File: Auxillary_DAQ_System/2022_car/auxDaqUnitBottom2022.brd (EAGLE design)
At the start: 121.9 x 193 mm, 120 parts, among them IC1 ADS8332IBPWR, IC2 ADS8332IBPWR, IC3 ADS8332IBPWR, IC4 XBEE, IC6 REG_3V3_LM3940, U1 REF5040AIDR, U3 TS1874IPT, U4 TS1874IPT, U5 TS1874IPT, U6 TS1874IPT, U7 TS1874IPT, U8 TS1874IPT

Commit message: Added missing capacitor values
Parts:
- C33, C34, C35, C36, C37, C38: value (none) -> .1uf
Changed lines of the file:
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@@
 <drawing>
 <settings>
-<setting alwaysvectorfont="yes"/>
+<setting alwaysvectorfont="no"/>
 <setting verticaltext="up"/>
 </settings>
@@
 <attribute name="VALUE" x="24.765" y="81.8515" size="1.27" layer="27" rot="R90"/>
 </element>
-<element name="C33" library="GTOR - Passive Components" package="C0603" package3d_urn="urn:adsk.eagle:package:23616/2" value="" x="21.59" y="163.195" smashed="yes" rot="R90">
+<element name="C33" library="GTOR - Passive Components" package="C0603" package3d_urn="urn:adsk.eagle:package:23616/2" value=".1uf" x="21.59" y="163.195" smashed="yes" rot="R90">
 <attribute name="NAME" x="20.955" y="162.56" size="1.27" layer="25" rot="R90"/>
 <attribute name="POPULARITY" value="73" x="21.59" y="163.195" size="1.778" layer="27" rot="R90" display="off"/>
@@
 <attribute name="VALUE" x="23.495" y="162.56" size="1.27" layer="27" rot="R90"/>
 </element>
-<element name="C34" library="GTOR - Passive Components" package="C0603" package3d_urn="urn:adsk.eagle:package:23616/2" value="" x="21.59" y="79.375" smashed="yes" rot="R90">
+<element name="C34" library="GTOR - Passive Components" package="C0603" package3d_urn="urn:adsk.eagle:package:23616/2" value=".1uf" x="21.59" y="79.375" smashed="yes" rot="R90">
 <attribute name="NAME" x="20.955" y="78.74" size="1.27" layer="25" rot="R90"/>
 <attribute name="POPULARITY" value="73" x="21.59" y="79.375" size="1.778" layer="27" rot="R90" display="off"/>
@@
 <attribute name="VALUE" x="23.495" y="78.74" size="1.27" layer="27" rot="R90"/>
 </element>
-<element name="C35" library="GTOR - Passive Components" package="C0603" package3d_urn="urn:adsk.eagle:package:23616/2" value="" x="21.59" y="118.745" smashed="yes" rot="R90">
+<element name="C35" library="GTOR - Passive Components" package="C0603" package3d_urn="urn:adsk.eagle:package:23616/2" value=".1uf" x="21.59" y="118.745" smashed="yes" rot="R90">
 <attribute name="NAME" x="20.955" y="118.11" size="1.27" layer="25" rot="R90"/>
 <attribute name="POPULARITY" value="73" x="21.59" y="118.745" size="1.778" layer="27" rot="R90" display="off"/>
@@
 <attribute name="VALUE" x="23.495" y="118.11" size="1.27" layer="27" rot="R90"/>
 </element>
-<element name="C36" library="GTOR - Passive Components" package="C0603" package3d_urn="urn:adsk.eagle:package:23616/2" value="" x="23.8125" y="163.195" smashed="yes" rot="R90">
+<element name="C36" library="GTOR - Passive Components" package="C0603" package3d_urn="urn:adsk.eagle:package:23616/2" value=".1uf" x="23.8125" y="163.195" smashed="yes" rot="R90">
 <attribute name="NAME" x="23.1775" y="162.56" size="1.27" layer="25" rot="R90"/>
 <attribute name="POPULARITY" value="73" x="23.8125" y="163.195" size="1.778" layer="27" rot="R90" display="off"/>
@@
 <attribute name="VALUE" x="25.7175" y="162.56" size="1.27" layer="27" rot="R90"/>
 </element>
-<element name="C37" library="GTOR - Passive Components" package="C0603" package3d_urn="urn:adsk.eagle:package:23616/2" value="" x="23.8125" y="79.375" smashed="yes" rot="R90">
+<element name="C37" library="GTOR - Passive Components" package="C0603" package3d_urn="urn:adsk.eagle:package:23616/2" value=".1uf" x="23.8125" y="79.375" smashed="yes" rot="R90">
 <attribute name="NAME" x="23.1775" y="78.74" size="1.27" layer="25" rot="R90"/>
 <attribute name="POPULARITY" value="73" x="23.8125" y="79.375" size="1.778" layer="27" rot="R90" display="off"/>
@@
 <attribute name="VALUE" x="25.7175" y="78.74" size="1.27" layer="27" rot="R90"/>
 </element>
-<element name="C38" library="GTOR - Passive Components" package="C0603" package3d_urn="urn:adsk.eagle:package:23616/2" value="" x="23.8125" y="118.745" smashed="yes" rot="R90">
+<element name="C38" library="GTOR - Passive Components" package="C0603" package3d_urn="urn:adsk.eagle:package:23616/2" value=".1uf" x="23.8125" y="118.745" smashed="yes" rot="R90">
 <attribute name="NAME" x="23.1775" y="118.11" size="1.27" layer="25" rot="R90"/>
 <attribute name="POPULARITY" value="73" x="23.8125" y="118.745" size="1.778" layer="27" rot="R90" display="off"/>

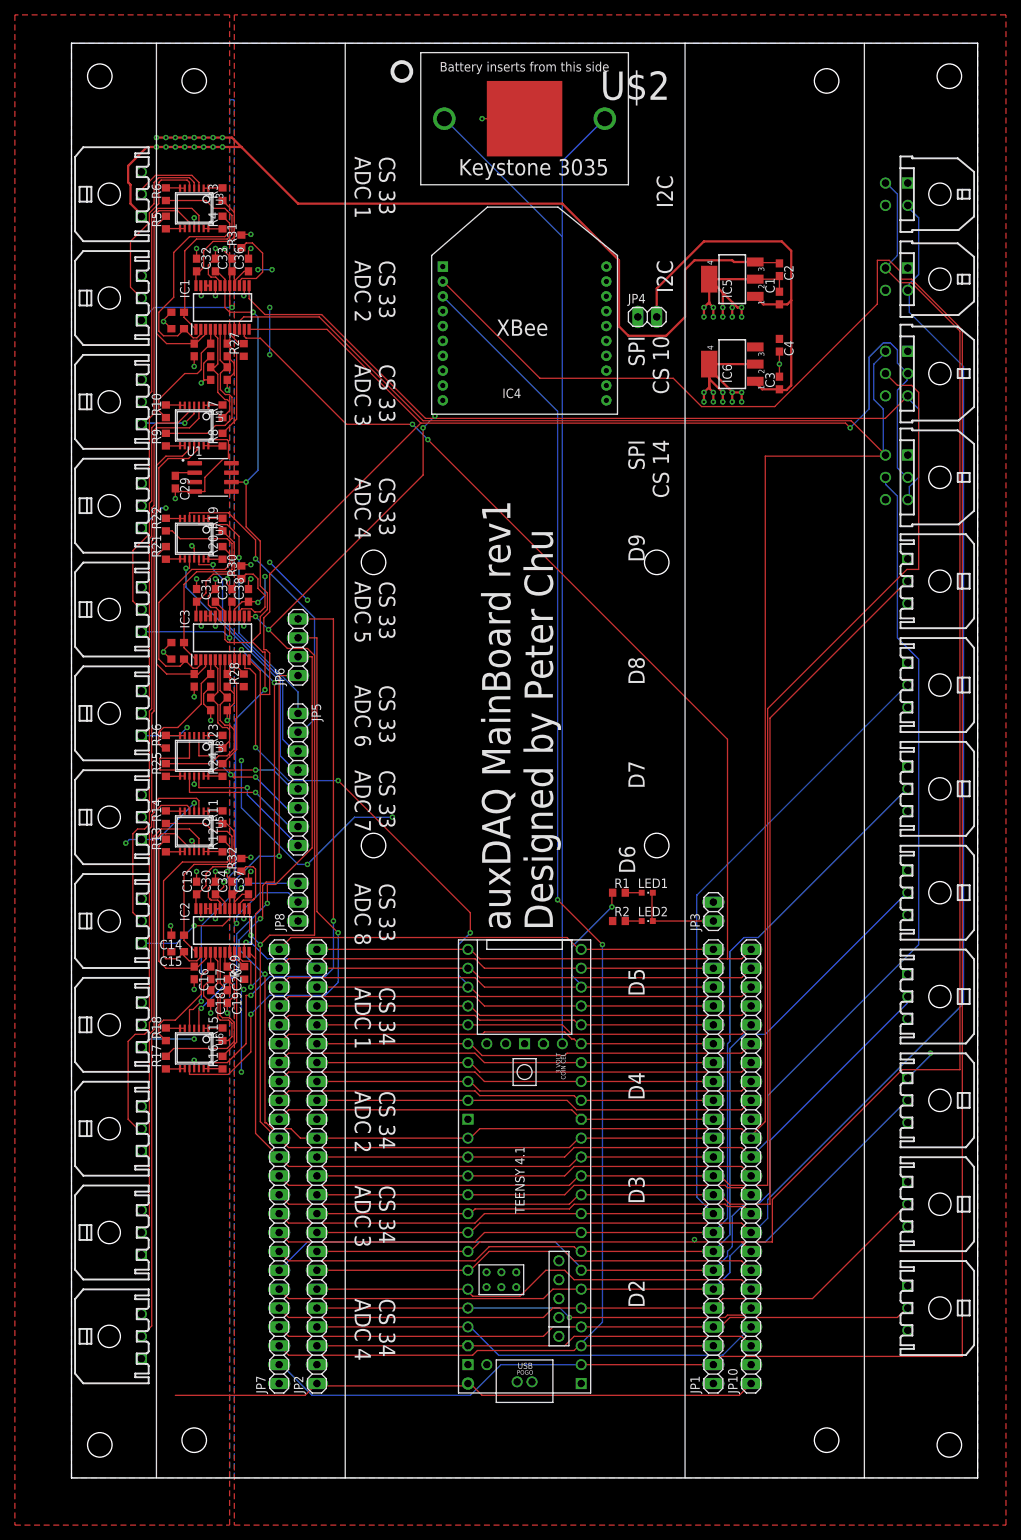
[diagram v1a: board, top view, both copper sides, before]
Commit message: Started changes for new Aux Daq
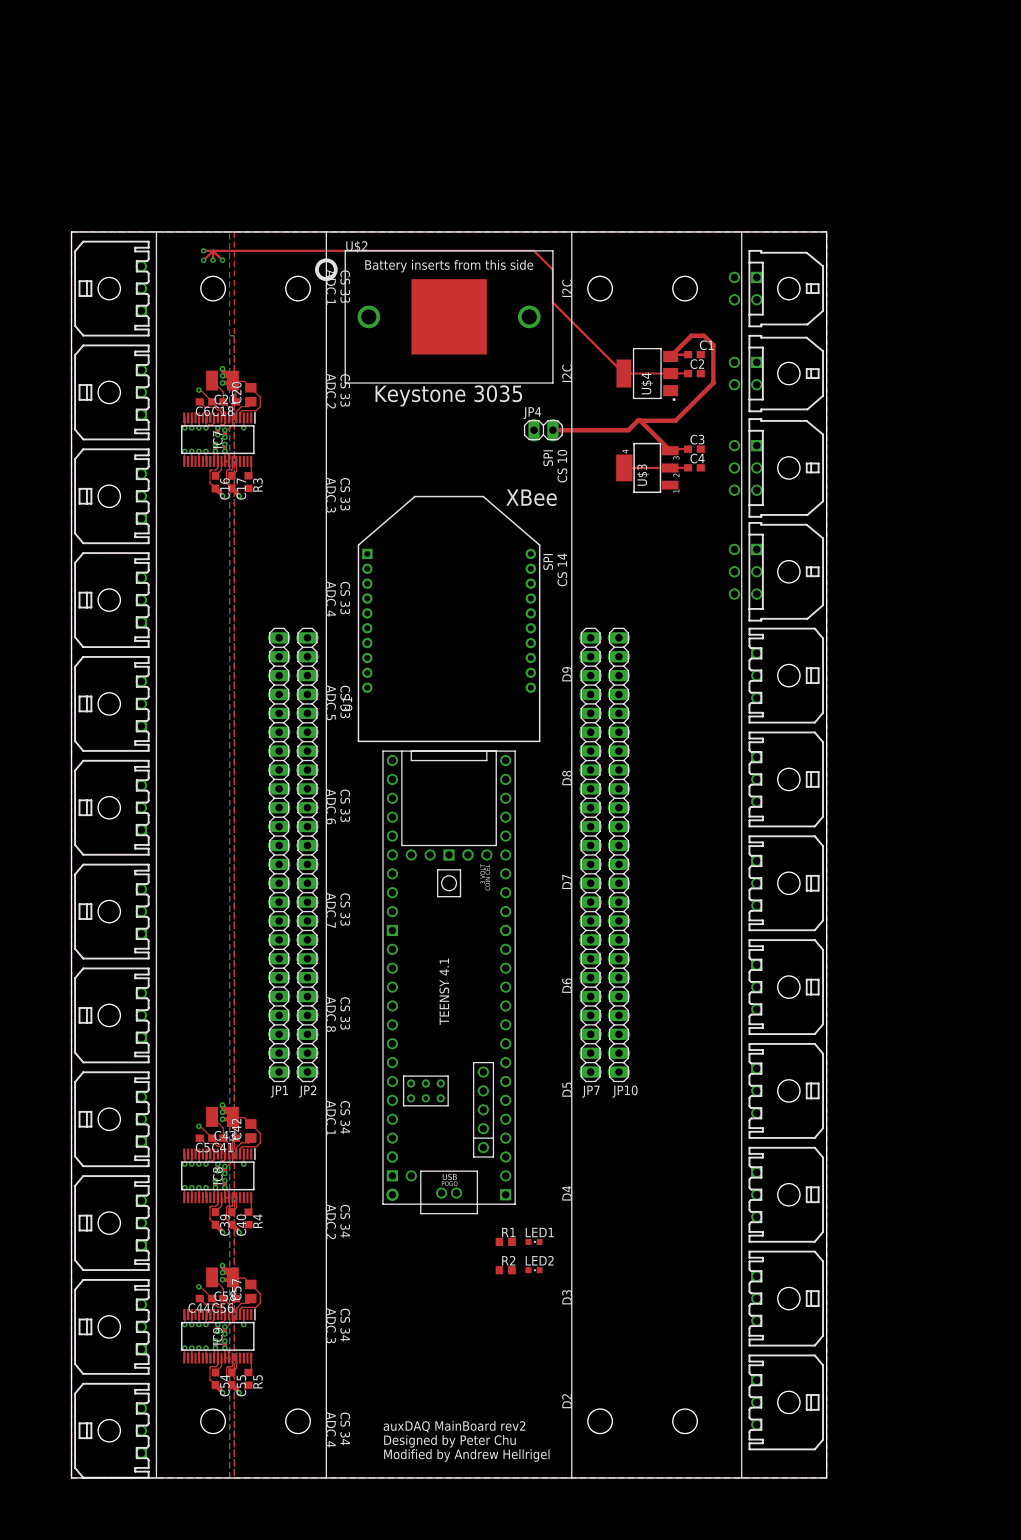
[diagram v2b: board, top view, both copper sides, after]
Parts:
- removed C10, C11, C12, C13, C14, C15, C19, C22, C23, C24, C25, C26, C27, C28, C7, C8, C9: 1nf, GTOR - Passive Components:C0603
- removed C29: 1uf, GTOR - Passive Components:C0603
- removed C30, C31, C32: 10uf, GTOR - Passive Components:C0603
- removed C33, C34, C35, C36, C37, C38: .1uf, GTOR - Passive Components:C0603
- removed IC1, IC2, IC3: ADS8332IBPWR, GTOR - Active Components:SOP65P640X120-24N
- removed IC4: XBEE, GTOR - Microcontroller:XBEE
- removed IC5: (no value), GTOR - Active Components:SOT223
- removed IC6: REG_3V3_LM3940, GTOR - Active Components:SOT223
- removed JP3: (no value), GTOR - Connectors:1X02
- removed JP5: (no value), GTOR - Connectors:1X08
- removed JP6: (no value), GTOR - Connectors:1X04
- removed JP8: (no value), GTOR - Connectors:1X03
- removed R10, R11, R12, R13, R14, R15, R16, R17, R18, R19, R20, R21, R22, R23, R24, R25, R26, R6, R7, R8, R9: 20, GTOR - Passive Components:R0603
- removed R27, R28, R29, R30, R31, R32: 10k, GTOR - Passive Components:R0603
- removed U3, U4, U5, U6, U7, U8: TS1874IPT, GTOR - Active Components:TSSOP14
- added C39, C41, C44, C54, C56: 1uF, GTOR - Passive Components:C0603
- added C40, C55: 10uF, GTOR - Passive Components:C0603
- added C42, C57: 10uF, GTOR - Passive Components:C0805
- added C43, C58: 22uF, GTOR - Passive Components:C1210
- added IC7, IC8, IC9: ADC_ADS8688IDBTR, GTOR - Active Components:SOP50P640X120-38N
- added U$3: REG_3V3_LMS8117A, GTOR - Active Components:SOT223
- added U$4: REG_5V_LDL1117S50R, GTOR - Active Components:SOT230P700X180-4N
- C16, C18, C5, C6: value 1nf -> 1uF
- C17: value 1nf -> 10uF
- C20: value 1nf -> 10uF; device GTOR - Passive Components:C0603 -> GTOR - Passive Components:C0805
- C21: value 1nf -> 22uF; device GTOR - Passive Components:C0603 -> GTOR - Passive Components:C1210
- R3, R4, R5: value 20 -> 10k
- U1: value REF5040AIDR -> XBEE_PRO_S3B; device GTOR - Active Components:SOIC127P599X175-8N -> GTOR - Microcontroller:XBEE_PRO_S3B
- moved R5 156.0 mm to (23.8, 13.3), turned to 270 degrees
- moved R4 134.0 mm to (23.8, 34.9), turned to 270 degrees
- moved C5 117.5 mm to (18.1, 45.7), turned to 180 degrees
- moved C18 80.1 mm to (21.3, 144.8), turned to 180 degrees
- moved C20 77.9 mm to (24.1, 145.7), turned to 90 degrees
- moved JP1 71.9 mm to (27.9, 83.8)
- moved C16 66.1 mm to (19.4, 134.0)
- moved C17 66.1 mm to (21.6, 134.0)
- moved JP7 59.3 mm to (69.8, 83.8)
- moved LED2 49.4 mm to (62.2, 27.9)
- moved R2 49.4 mm to (58.4, 27.9)
- moved LED1 49.4 mm to (62.2, 31.8)
- moved R1 49.4 mm to (58.4, 31.8)
- moved JP10 45.5 mm to (73.7, 83.8)
- moved JP2 41.9 mm to (31.8, 83.8)
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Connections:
- removed net IN1: C5.1, IC1.24, R3.1
- removed net IN10: C14.1, IC2.1, R14.1
- removed net IN11: C15.1, IC2.2, R12.2
- removed net IN12: C16.1, IC2.3, R13.2
- removed net IN13: C17.1, IC2.4, R18.1
- removed net IN14: C18.1, IC2.5, R15.1
- removed net IN15: C19.1, IC2.6, R17.2
- removed net IN16: C20.1, IC2.7, R16.2
- removed net IN17: C21.1, IC3.24, R19.1
- removed net IN18: C22.1, IC3.1, R22.1
- removed net IN19: C23.1, IC3.2, R20.2
- removed net IN2: C6.1, IC1.1, R6.1
- removed net IN20: C24.1, IC3.3, R21.2
- removed net IN21: C25.1, IC3.4, R26.1
- removed net IN22: C26.1, IC3.5, R23.1
- removed net IN23: C27.1, IC3.6, R25.2
- removed net IN24: C28.1, IC3.7, R24.2
- removed net IN3: C7.1, IC1.2, R4.2
- removed net IN4: C8.1, IC1.3, R5.2
- removed net IN5: C9.1, IC1.4, R10.1
- removed net IN6: C10.1, IC1.5, R7.1
- removed net IN7: C11.1, IC1.6, R9.2
- removed net IN8: C12.1, IC1.7, R8.2
- removed net IN9: C13.1, IC2.24, R11.1
- removed net N$10: IC1.8, R27.2
- removed net N$11: R7.2, U4.1, U4.2
- removed net N$12: R10.2, U4.6, U4.7
- removed net N$14: R8.1, U4.13, U4.14
- removed net N$15: IC3.8, R28.2
- removed net N$16: R11.2, U5.1, U5.2
- removed net N$18: R13.1, U5.8, U5.9
- removed net N$19: R12.1, U5.13, U5.14
- removed net N$20: IC2.8, R29.2
- removed net N$21: R15.2, U6.1, U6.2
- removed net N$22: R18.2, U6.6, U6.7
- removed net N$23: R17.1, U6.8, U6.9
- removed net N$24: R16.1, U6.13, U6.14
- removed net N$25: IC3.15, R30.1
- removed net N$26: R19.2, U7.1, U7.2
- removed net N$27: R22.2, U7.6, U7.7
- removed net N$29: R20.1, U7.13, U7.14
- removed net N$3: IC1.21, IC1.22
- removed net N$30: IC1.15, R31.1
- removed net N$33: R25.1, U8.8, U8.9
- removed net N$34: R24.1, U8.13, U8.14
- removed net N$35: IC2.15, R32.1
- removed net N$4: IC2.21, IC2.22
- removed net N$5: IC3.21, IC3.22
- removed net N$9: R4.1, U3.13, U3.14
- removed net REF+: C30.1, C31.1, C32.1, IC1.18, IC2.18, IC3.18, U1.6
- new net N$45: C57.1, IC9.5
- new net NC1: IC7.35
- new net NC2: IC8.35
- new net NC3: IC9.35
- net +12V: now also U$3.3, U$4.3; no longer IC5.1, IC6.1
- net +3V3: now also C17.1, C40.1, C55.1, IC7.2, IC7.34, IC8.2, IC8.34, IC9.2, IC9.34, JP10.3, JP2.3, R3.2, R4.2, R5.2, U$3.2, U$3.4, U1.1; no longer C36.1, C37.1, C38.1, IC1.16, IC2.16, IC3.16, IC4.1, IC6.3, JP3.2, JP8.2, R27.1, R28.1, R29.1
- net +5V: now also C16.1, C39.1, C44.2, C5.2, C54.1, C6.2, IC7.30, IC7.9, IC8.30, IC8.9, IC9.30, IC9.9, U$4.2, U$4.4; no longer C29.1, C33.1, C34.1, C35.1, IC1.17, IC2.17, IC3.17, IC5.3, JP8.3, U1.2, U3.4, U4.4, U5.4, U6.4, U7.4, U8.4
- net 10: no longer JP1.12
- net 2: no longer JP1.4
- net 3: no longer JP1.5
- net 33: now also IC7.38, R3.1; no longer IC1.11
- net 34: now also IC8.38, R4.1; no longer IC2.11
- net 35: now also IC9.38, R5.1; no longer IC3.11
- net 3V3-3: no longer JP10.3, JP2.3
- net 4: no longer JP1.6
- net 5: no longer JP1.7
- net 6: no longer JP1.8
- net 7: no longer JP1.9
- net 8: no longer JP1.10
- net 9: no longer JP1.11
- net ADC1: now also IC7.16; no longer U3.3
- net ADC10: now also IC8.18; no longer U5.5
- net ADC11: now also IC8.21; no longer U5.12
- net ADC12: now also IC8.23; no longer U5.10
- net ADC13: now also IC8.25, JP1.1; no longer JP6.1, U6.5
- net ADC14: now also IC8.27, JP1.2; no longer JP6.2, U6.3
- net ADC15: now also IC8.12, JP1.3; no longer JP6.3, U6.10
- net ADC16: now also IC8.14, JP1.4; no longer JP6.4, U6.12
- net ADC17: now also IC9.16, JP1.5; no longer JP5.1, U7.3
- net ADC18: now also IC9.18, JP1.6; no longer JP5.2, U7.5
- net ADC19: now also IC9.21, JP1.7; no longer JP5.3, U7.12
- net ADC2: now also IC7.18; no longer U3.5
- net ADC20: now also IC9.23, JP1.8; no longer JP5.4, U7.10
- net ADC21: now also IC9.25, JP1.9; no longer JP5.5, U8.5
- net ADC22: now also IC9.27, JP1.10; no longer JP5.6, U8.3
- net ADC23: now also IC9.12, JP1.11; no longer JP5.7, U8.10
- net ADC24: now also IC9.14, JP1.12; no longer JP5.8, U8.12
- net ADC3: now also IC7.21; no longer U3.12
- net ADC4: now also IC7.23; no longer U3.10
- net ADC5: now also IC7.25; no longer U4.5
- net ADC6: now also IC7.27; no longer U4.3
- net ADC7: now also IC7.12; no longer U4.10
- net ADC8: now also IC7.14; no longer U4.12
- net ADC9: now also IC8.16; no longer U5.3
- net GND: now also C18.1, C21.1, C39.2, C40.2, C41.1, C42.2, C43.1, C44.1, C5.1, C54.2, C55.2, C56.1, C57.2, C58.1, C6.1, IC7.11, IC7.13, IC7.15, IC7.17, IC7.19, IC7.20, IC7.22, IC7.24, IC7.26, IC7.28, IC7.29, IC7.3, IC7.31, IC7.32, IC7.33, IC7.4, IC7.6, IC7.8, IC8.11, IC8.13, IC8.15, IC8.17, IC8.19, IC8.20, IC8.22, IC8.24, IC8.26, IC8.28, IC8.29, IC8.3, IC8.31, IC8.32, IC8.33, IC8.4, IC8.6, IC8.8, IC9.11, IC9.13, IC9.15, IC9.17, IC9.19, IC9.20, IC9.22, IC9.24, IC9.26, IC9.28, IC9.29, IC9.3, IC9.31, IC9.32, IC9.33, IC9.4, IC9.6, IC9.8, U$3.1, U$4.1, U1.10; no longer C10.2, C11.2, C12.2, C13.2, C14.2, C15.2, C18.2, C19.2, C21.2, C22.2, C23.2, C24.2, C25.2, C26.2, C27.2, C28.2, C29.2, C30.2, C31.2, C32.2, C33.2, C34.2, C35.2, C36.2, C37.2, C38.2, C5.2, C6.2, C7.2, C8.2, C9.2, IC1.14, IC1.19, IC1.20, IC1.23, IC2.14, IC2.19, IC2.20, IC2.23, IC3.14, IC3.19, IC3.20, IC3.23, IC4.10, IC5.2, IC5.4, IC6.2, IC6.4, JP1.1, JP3.1, JP8.1, R30.2, R31.2, R32.2, U1.4, U3.11, U4.11, U5.11, U6.11, U7.11, U8.11
- net MISO: now also IC7.36, IC8.36, IC9.36; no longer IC1.13, IC2.13, IC3.13
- net MOSI: now also IC7.1, IC8.1, IC9.1; no longer IC1.12, IC2.12, IC3.12
- net N$13: now also C18.2, C21.2, IC7.7; no longer R9.1, U4.8, U4.9
- net N$17: now also IC7.10; no longer R14.2, U5.6, U5.7
- net N$28: now also C42.1, IC8.5; no longer R21.1, U7.8, U7.9
- net N$31: now also C56.2, C58.2, IC9.7; no longer R23.2, U8.1, U8.2
- net N$32: now also IC9.10; no longer R26.2, U8.6, U8.7
- net N$6: now also C20.1, IC7.5; no longer R3.2, U3.1, U3.2
- net N$7: now also C41.2, C43.2, IC8.7; no longer R6.2, U3.6, U3.7
- net N$8: now also IC8.10; no longer R5.1, U3.8, U3.9
- net SCK: now also IC7.37, IC8.37, IC9.37; no longer IC1.10, IC2.10, IC3.10
- net XBEE_DIN: now also U1.3; no longer IC4.3, JP1.3
- net XBEE_DOUT: now also U1.2; no longer IC4.2, JP1.2
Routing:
- net SCK: track 367.0 -> 0.00 mm, vias 5 -> 0
- net XBEE_DOUT: track 326.9 -> 0.00 mm
- net MISO: track 300.7 -> 0.00 mm, vias 6 -> 0
- net MOSI: track 297.8 -> 0.00 mm, vias 1 -> 0
- net +5V: track 328.0 -> 99.2 mm, vias 26 -> 4
- net SCL: track 228.0 -> 0.00 mm, vias 1 -> 0
- net SDA: track 214.2 -> 0.00 mm
- net XBEE_DIN: track 210.7 -> 0.00 mm, vias 2 -> 0
- net 10: track 188.8 -> 0.00 mm
- net 33: track 177.4 -> 2.08 mm, vias 2 -> 0
- net 14: track 162.1 -> 0.00 mm
- net 9: track 159.2 -> 0.00 mm
- net VBAT: track 149.3 -> 0.00 mm
- net 8: track 143.3 -> 0.00 mm
- net 7: track 131.2 -> 0.00 mm
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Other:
- board size 121.9 x 193 mm -> 101.6 x 167.6 mm
- board text added: "auxDAQ MainBoard rev2 Designed by Peter Chu Modified by Andrew Hellrigel"
- board text removed: "Power"
- board text removed: "auxDAQ MainBoard rev1 Designed by Peter Chu"

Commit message: Finished routing aux daq
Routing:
- net MOSI: track 0.00 -> 267.7 mm, vias 0 -> 7
- net MISO: track 0.00 -> 264.1 mm, vias 0 -> 9
- net SCK: track 0.00 -> 250.4 mm, vias 0 -> 5
- net +5V: track 99.2 -> 284.4 mm, vias 4 -> 23
- net SCL: track 0.00 -> 162.1 mm, vias 0 -> 2
- net SDA: track 0.00 -> 161.0 mm, vias 0 -> 2
- net 35: track 2.08 -> 162.9 mm, vias 0 -> 4
- net 34: track 2.08 -> 135.1 mm, vias 0 -> 5
- net XBEE_DIN: track 0.00 -> 125.7 mm, vias 0 -> 2
- net 30: track 0.00 -> 124.4 mm, vias 0 -> 4
- net ADC8: track 0.00 -> 123.8 mm, vias 0 -> 1
- net 14: track 0.00 -> 118.9 mm, vias 0 -> 6
- net 10: track 0.00 -> 104.6 mm, vias 0 -> 4
- net XBEE_DOUT: track 0.00 -> 104.4 mm, vias 0 -> 3
- net ADC22: track 0.00 -> 100.9 mm, vias 0 -> 2
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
